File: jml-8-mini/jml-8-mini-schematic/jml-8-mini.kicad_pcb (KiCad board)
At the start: 4 copper layers, 136.4 x 81.5 mm, 50 parts, among them J1 BarrelJack, J2 SIO CHB, J3 UART, J4 CTC Extra Lines, J5 Address Decoding, J6 Z80 Lines, SW1 Reset, SW2 Power, U1 Z80CPU, U10 74LS74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

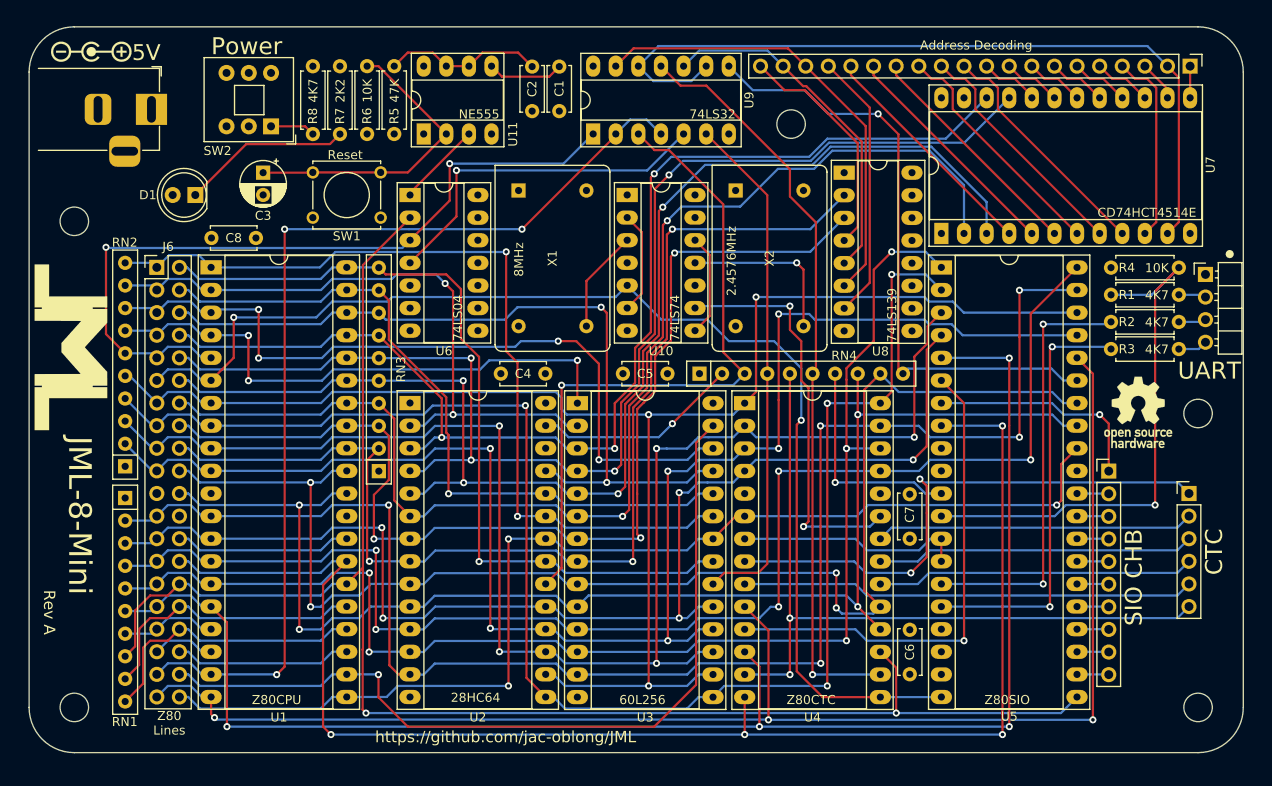
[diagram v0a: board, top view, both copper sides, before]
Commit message: add ground plane to top and bottom, fix silkscreen, regenerate gerbers
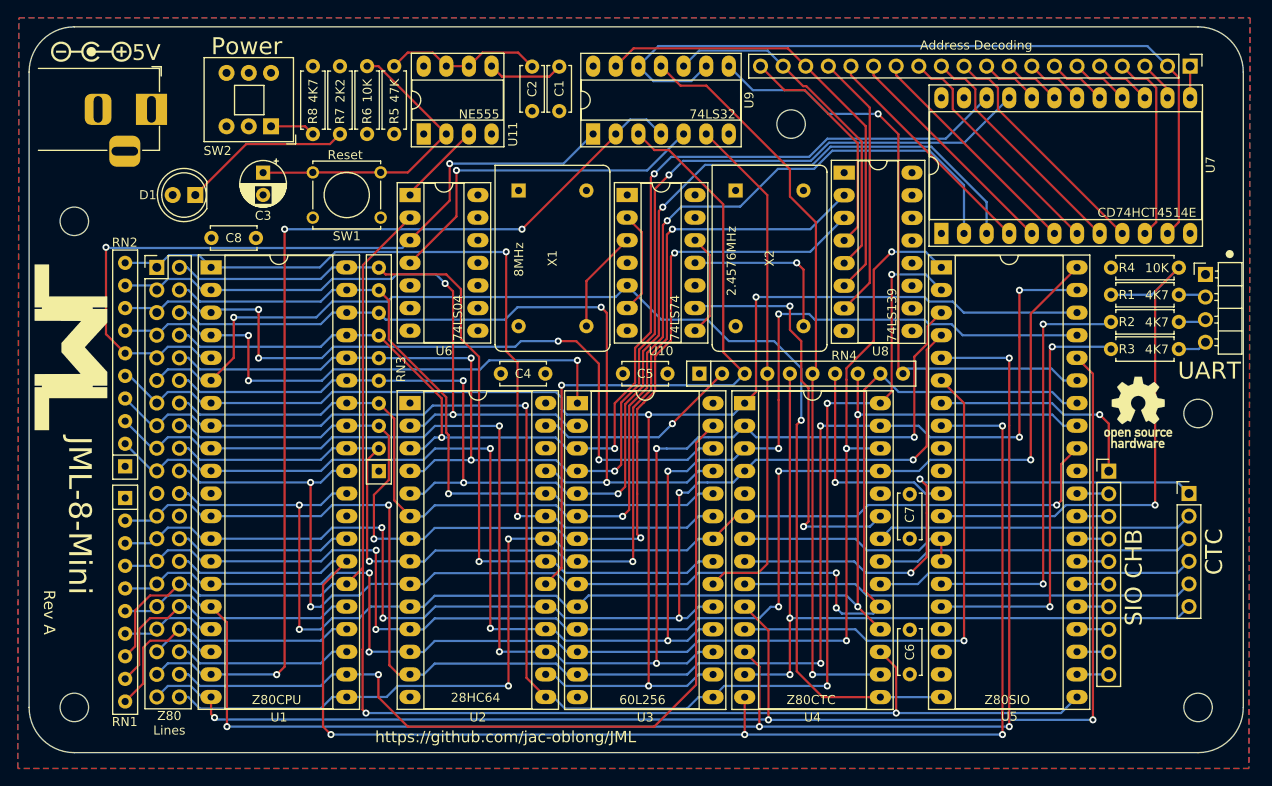
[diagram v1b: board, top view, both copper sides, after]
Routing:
- added copper zone on B.Cu, net GND
- added copper zone on F.Cu, net GND
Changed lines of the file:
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@@
       (net 70 "/~{RFSH}") (pinfunction "~{RFSH}") (pintype "output"))
     (pad "29" thru_hole oval (at 15.24 27.94) (size 2.4 1.6) (drill 0.8) (layers "*.Cu" "*.Mask")
-      (net 1 "GND") (pinfunction "GND") (pintype "power_in"))
+      (net 1 "GND") (pinfunction "GND") (pintype "power_in") (zone_connect 2))
     (pad "30" thru_hole oval (at 15.24 25.4) (size 2.4 1.6) (drill 0.8) (layers "*.Cu" "*.Mask")
       (net 67 "/A0") (pinfunction "A0") (pintype "output"))
@@
       (stroke (width 0.1) (type solid)) (layer "F.Fab"))
     (pad "1" thru_hole rect (at 0 0 90) (size 2.4 1.6) (drill 0.8) (layers "*.Cu" "*.Mask")
-      (net 1 "GND") (pinfunction "GND") (pintype "power_in"))
+      (net 1 "GND") (pinfunction "GND") (pintype "power_in") (zone_connect 2))
     (pad "2" thru_hole oval (at 0 2.54 90) (size 2.4 1.6) (drill 0.8) (layers "*.Cu" "*.Mask")
       (net 4 "/Power, Clock and Reset/555Trigger") (pinfunction "TR") (pintype "input"))
@@
       (net 68 "/D2") (pinfunction "D2") (pintype "bidirectional"))
     (pad "14" thru_hole oval (at 0 33.02) (size 2.4 1.6) (drill 0.8) (layers "*.Cu" "*.Mask")
-      (net 1 "GND") (pinfunction "GND") (pintype "power_in"))
+      (net 1 "GND") (pinfunction "GND") (pintype "power_in") (zone_connect 2))
     (pad "15" thru_hole oval (at 15.24 33.02) (size 2.4 1.6) (drill 0.8) (layers "*.Cu" "*.Mask")
       (net 61 "/D3") (pinfunction "D3") (pintype "bidirectional"))
@@
       (net 54 "/A7") (pinfunction "A3") (pintype "input"))
     (pad "23" thru_hole oval (at 15.24 2.54 90) (size 2.4 1.6) (drill 0.8) (layers "*.Cu" "*.Mask")
-      (net 1 "GND") (pinfunction "~{E}") (pintype "input"))
+      (net 1 "GND") (pinfunction "~{E}") (pintype "input") (zone_connect 2))
     (pad "24" thru_hole oval (at 15.24 0 90) (size 2.4 1.6) (drill 0.8) (layers "*.Cu" "*.Mask")
       (net 5 "+5V") (pinfunction "VCC") (pintype "input"))
@@
       (net 12 "/Peripherals/~{W}{slash}~{RDYB}") (pinfunction "~{W}/~{RDYB}") (pintype "output"))
     (pad "31" thru_hole oval (at 15.24 22.86) (size 2.4 1.6) (drill 0.8) (layers "*.Cu" "*.Mask")
-      (net 1 "GND") (pinfunction "GND") (pintype "power_in"))
+      (net 1 "GND") (pinfunction "GND") (pintype "power_in") (zone_connect 2))
     (pad "32" thru_hole oval (at 15.24 20.32) (size 2.4 1.6) (drill 0.8) (layers "*.Cu" "*.Mask")
       (net 84 "/~{RD}") (pinfunction "~{RD}") (pintype "input"))
@@
       (net 5 "+5V") (pintype "passive"))
     (pad "2" thru_hole circle (at 5 0 180) (size 1.6 1.6) (drill 0.8) (layers "*.Cu" "*.Mask")
-      (net 1 "GND") (pintype "passive"))
+      (net 1 "GND") (pintype "passive") (zone_connect 2))
     (model "${KICAD6_3DMODEL_DIR}/Capacitor_THT.3dshapes/C_Disc_D5.0mm_W2.5mm_P5.00mm.wrl"
       (offset (xyz 0 0 0))
@@
       (net 92 "/~{RAM}") (pintype "output"))
     (pad "7" thru_hole oval (at 0 15.24 90) (size 2.4 1.6) (drill 0.8) (layers "*.Cu" "*.Mask")
-      (net 1 "GND") (pinfunction "GND") (pintype "power_in"))
+      (net 1 "GND") (pinfunction "GND") (pintype "power_in") (zone_connect 2))
     (pad "8" thru_hole oval (at 7.62 15.24 90) (size 2.4 1.6) (drill 0.8) (layers "*.Cu" "*.Mask")
       (net 94 "/~{SIO}") (pintype "output"))
@@
     (property "ki_keywords" "connector")
     (attr through_hole)
-    (fp_text reference "J6" (at 1.27 -2.33 unlocked) (layer "F.SilkS")
+    (fp_text reference "J6" (at 1.27 -2.33 unlocked) (layer "F.SilkS") hide
         (effects (font (size 1.016 1.016) (thickness 0.1524)))
     )
@@
       (net 108 "unconnected-(U6-Pad8)") (pintype "output+no_connect"))
     (pad "9" thru_hole oval (at 7.62 12.7) (size 2.4 1.6) (drill 0.8) (layers "*.Cu" "*.Mask")
-      (net 1 "GND") (pintype "input"))
+      (net 1 "GND") (pintype "input") (zone_connect 2))
     (pad "10" thru_hole oval (at 7.62 10.16) (size 2.4 1.6) (drill 0.8) (layers "*.Cu" "*.Mask")
       (net 109 "unconnected-(U6-Pad10)") (pintype "output+no_connect"))
     (pad "11" thru_hole oval (at 7.62 7.62) (size 2.4 1.6) (drill 0.8) (layers "*.Cu" "*.Mask")
-      (net 1 "GND") (pintype "input"))
+      (net 1 "GND") (pintype "input") (zone_connect 2))
     (pad "12" thru_hole oval (at 7.62 5.08) (size 2.4 1.6) (drill 0.8) (layers "*.Cu" "*.Mask")
       (net 110 "unconnected-(U6-Pad12)") (pintype "output+no_connect"))
     (pad "13" thru_hole oval (at 7.62 2.54) (size 2.4 1.6) (drill 0.8) (layers "*.Cu" "*.Mask")
-      (net 1 "GND") (pintype "input"))
+      (net 1 "GND") (pintype "input") (zone_connect 2))
     (pad "14" thru_hole oval (at 7.62 0) (size 2.4 1.6) (drill 0.8) (layers "*.Cu" "*.Mask")
       (net 5 "+5V") (pinfunction "VCC") (pintype "power_in"))
@@
   (via (at 170.053 76.546) (size 0.8) (drill 0.4) (layers "F.Cu" "B.Cu") (net 118))
   (segment (start 170.053 76.546) (end 158.628 76.546) (width 0.25) (layer "B.Cu") (net 118))
-  (zone (net 1) (net_name "GND") (layer "In1.Cu") (hatch edge 0.5)
+  (zone (net 0) (net_name "") (layer "F.Cu") (hatch full 0.5)
+    (connect_pads (clearance 0))
+    (min_thickness 0.25) (filled_areas_thickness no)
+    (keepout (tracks allowed) (vias allowed) (pads allowed) (copperpour not_allowed) (footprints allowed))
+    (fill (thermal_gap 0.5) (thermal_bridge_width 0.5))
+    (polygon
+      (pts
+        (xy 123.19 78.232)
+        (xy 123.317 85.09)
+        (xy 130.937 92.329)
+        (xy 131.064 78.105)
+      )
+    )
+  )
+  (zone (net 0) (net_name "") (layer "F.Cu") (hatch full 0.5)
+    (connect_pads (clearance 0))
+    (min_thickness 0.25) (filled_areas_thickness no)
+    (keepout (tracks allowed) (vias allowed) (pads allowed) (copperpour not_allowed) (footprints allowed))
+    (fill (thermal_gap 0.5) (thermal_bridge_width 0.5))
+    (polygon
+      (pts
+        (xy 149.098 80.518)
+        (xy 153.162 80.518)
+        (xy 153.162 91.567)
+        (xy 149.098 91.567)
+      )
+    )
+  )
+  (zone (net 1) (net_name "GND") (layers "F.Cu" "In1.Cu" "B.Cu") (hatch edge 0.5)
     (connect_pads (clearance 0.381))
     (min_thickness 0.254) (filled_areas_thickness no)
@@
       )
     )
+  )
+  (zone (net 0) (net_name "") (layer "B.Cu") (hatch full 0.5)
+    (connect_pads (clearance 0))
+    (min_thickness 0.25) (filled_areas_thickness no)
+    (keepout (tracks allowed) (vias allowed) (pads allowed) (copperpour not_allowed) (footprints allowed))
+    (fill (thermal_gap 0.5) (thermal_bridge_width 0.5))
+    (polygon
+      (pts
+        (xy 115.951 127.635)
+        (xy 160.02 127.508)
+        (xy 160.401 120.142)
+        (xy 129.667 121.666)
+        (xy 115.951 125.095)
+      )
+    )
+  )
+  (zone (net 0) (net_name "") (layer "B.Cu") (hatch full 0.5)
+    (connect_pads (clearance 0))
+    (min_thickness 0.25) (filled_areas_thickness no)
+    (keepout (tracks allowed) (vias allowed) (pads allowed) (copperpour not_allowed) (footprints allowed))
+    (fill (thermal_gap 0.5) (thermal_bridge_width 0.5))
+    (polygon
+      (pts
+        (xy 98.933 98.806)
+        (xy 98.806 107.188)
+        (xy 126.365 107.188)
+        (xy 126.492 98.679)
+      )
+    )
+  )
+  (zone (net 0) (net_name "") (layer "B.Cu") (hatch full 0.5)
+    (connect_pads (clearance 0))
+    (min_thickness 0.25) (filled_areas_thickness no)
+    (keepout (tracks allowed) (vias allowed) (pads allowed) (copperpour not_allowed) (footprints allowed))
+    (fill (thermal_gap 0.5) (thermal_bridge_width 0.5))
+    (polygon
+      (pts
+        (xy 164.084 101.219)
+        (xy 163.957 111.379)
+        (xy 160.147 111.379)
+        (xy 160.528 101.219)
+      )
+    )
